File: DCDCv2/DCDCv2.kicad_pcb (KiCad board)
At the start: 4 copper layers, 137.2 x 79 mm, 58 parts, among them M1 CSD18513Q5A, M1_2 CSD18513Q5A, M2 CSD18531Q5A, M3 CSD18533Q5A, M3_2 CSD18533Q5A, M4 CSD19534Q5A, M4_2 CSD19534Q5A, U1 LM5175PWPR

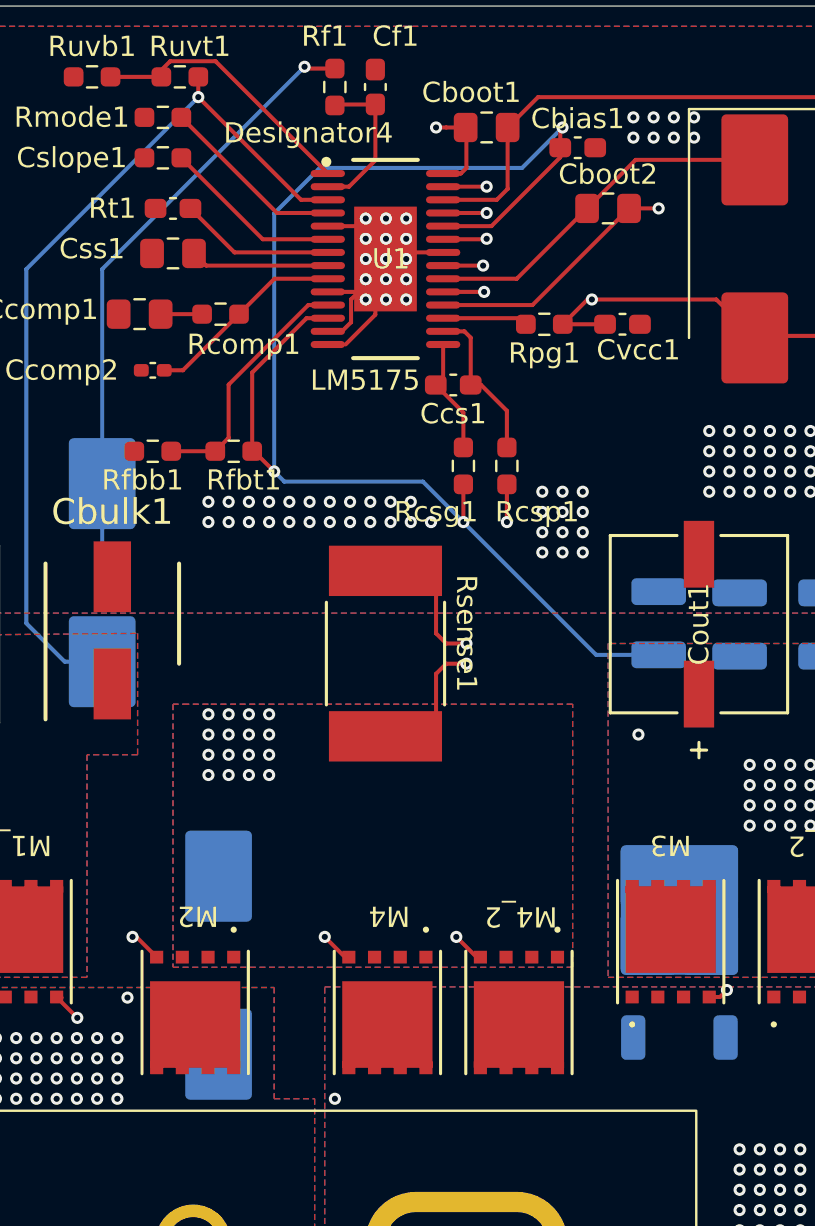
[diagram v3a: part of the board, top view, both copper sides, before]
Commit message: changed sw1 and sw2 to BCu layer
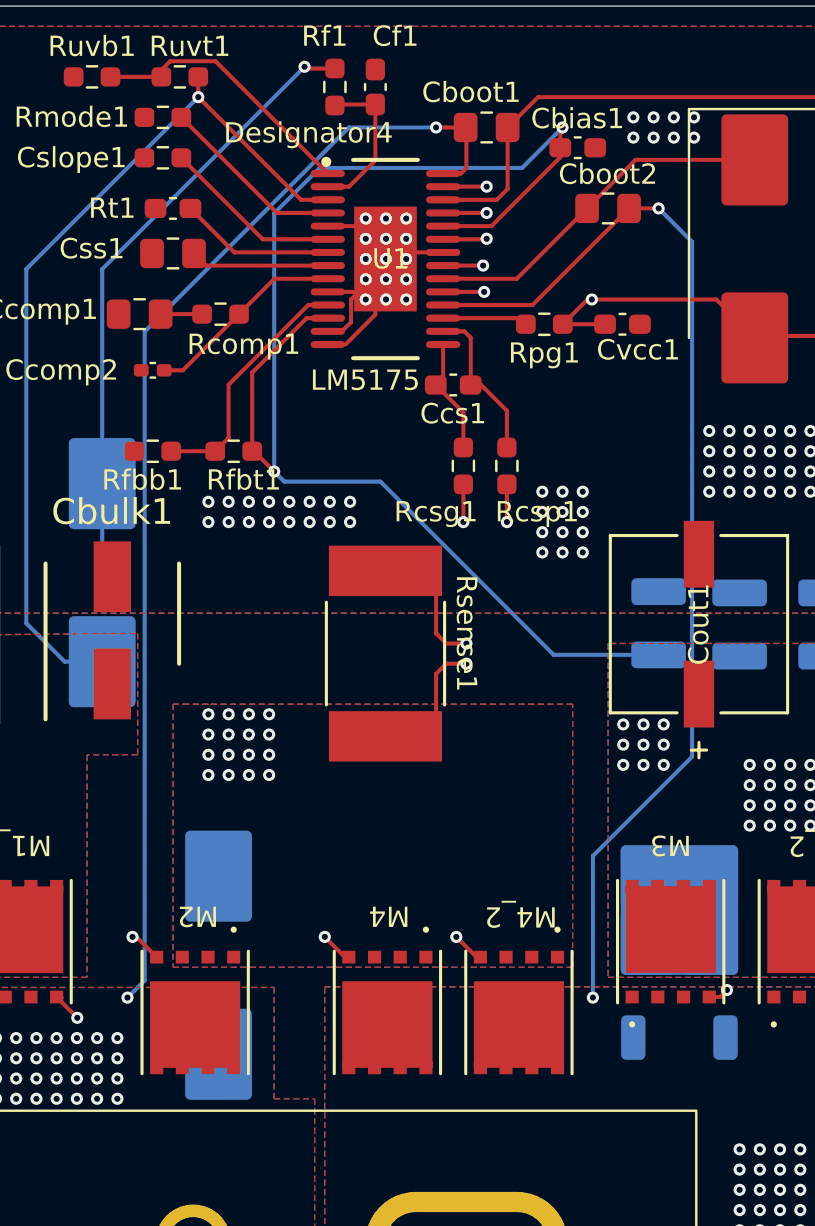
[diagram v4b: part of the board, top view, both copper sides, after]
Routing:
- net /sw2: track 88.0 -> 54.3 mm
- net /sw1: track 54.8 -> 56.6 mm
- net Vout: vias 99 -> 107
- net GND: vias 380 -> 373
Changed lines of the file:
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@@
 	)
 	(via micro
-		(at 95 54.5)
-		(size 0.6)
-		(drill 0.3)
-		(layers "F.Cu" "B.Cu")
-		(free yes)
-		(net 1)
-	)
-	(via micro
 		(at 39.25 50.5)
 		(size 0.6)
@@
 	)
 	(via micro
-		(at 93 54.5)
-		(size 0.6)
-		(drill 0.3)
-		(layers "F.Cu" "B.Cu")
-		(free yes)
-		(net 1)
-	)
-	(via micro
 		(at 147.75 52)
 		(size 0.6)
@@
 	)
 	(via micro
-		(at 96 54.5)
-		(size 0.6)
-		(drill 0.3)
-		(layers "F.Cu" "B.Cu")
-		(free yes)
-		(net 1)
-	)
-	(via micro
 		(at 52.25 52.5)
 		(size 0.6)
@@
 	)
 	(via micro
-		(at 94 54.5)
-		(size 0.6)
-		(drill 0.3)
-		(layers "F.Cu" "B.Cu")
-		(free yes)
-		(net 1)
-	)
-	(via micro
 		(at 47.25 52.5)
 		(size 0.6)
@@
 	)
 	(via micro
-		(at 94 53.5)
-		(size 0.6)
-		(drill 0.3)
-		(layers "F.Cu" "B.Cu")
-		(free yes)
-		(net 1)
-	)
-	(via micro
 		(at 49.25 52.5)
 		(size 0.6)
@@
 	)
 	(via micro
-		(at 95 53.5)
-		(size 0.6)
-		(drill 0.3)
-		(layers "F.Cu" "B.Cu")
-		(free yes)
-		(net 1)
-	)
-	(via micro
 		(at 113.75 53)
 		(size 0.6)
@@
 	)
 	(via micro
-		(at 93 53.5)
-		(size 0.6)
-		(drill 0.3)
-		(layers "F.Cu" "B.Cu")
-		(free yes)
-		(net 1)
-	)
-	(via micro
 		(at 114.75 52)
 		(size 0.6)
@@
 		(size 0.6)
 		(drill 0.3)
-		(layers "F.Cu" "In2.Cu")
+		(layers "F.Cu" "B.Cu")
 		(free yes)
 		(net 3)
@@
 		(size 0.6)
 		(drill 0.3)
-		(layers "F.Cu" "In2.Cu")
+		(layers "F.Cu" "B.Cu")
 		(net 3)
 	)
@@
 	)
 	(segment
-		(start 80.1 68.65)
-		(end 80.1 77.1)
-		(width 0.2)
-		(layer "In2.Cu")
-		(net 3)
-	)
-	(segment
-		(start 82.25 49)
-		(end 82.25 66.5)
+		(start 96.25 35)
+		(end 91.934314 35)
 		(width 0.2)
-		(layer "In2.Cu")
+		(layer "B.Cu")
 		(net 3)
 	)
 	(segment
-		(start 96.25 35)
-		(end 82.25 49)
+		(start 91.934314 35)
+		(end 81.85 45.084314)
 		(width 0.2)
-		(layer "In2.Cu")
+		(layer "B.Cu")
 		(net 3)
 	)
 	(segment
-		(start 82.25 66.5)
-		(end 80.1 68.65)
+		(start 81.85 45.084314)
+		(end 81.85 77.15)
 		(width 0.2)
-		(layer "In2.Cu")
+		(layer "B.Cu")
 		(net 3)
 	)
 	(segment
-		(start 80.1 77.1)
+		(start 81.85 77.15)
 		(end 81 78)
 		(width 0.2)
-		(layer "In2.Cu")
+		(layer "B.Cu")
 		(net 3)
 	)
@@
 		(size 0.6)
 		(drill 0.3)
-		(layers "F.Cu" "In2.Cu")
+		(layers "F.Cu" "B.Cu")
 		(net 5)
 	)
@@
 	)
 	(via micro
-		(at 91.25 83)
+		(at 104 78)
 		(size 0.6)
 		(drill 0.3)
-		(layers "F.Cu" "In2.Cu")
+		(layers "F.Cu" "B.Cu")
 		(free yes)
 		(net 5)
@@
 	)
 	(segment
-		(start 80.5 75.75)
-		(end 80.5 68.815686)
-		(width 0.2)
-		(layer "In2.Cu")
-		(net 5)
-	)
-	(segment
-		(start 80.5 68.815686)
-		(end 82.65 66.665686)
-		(width 0.2)
-		(layer "In2.Cu")
-		(net 5)
-	)
-	(segment
-		(start 82.65 66.665686)
-		(end 82.65 50.1)
-		(width 0.2)
-		(layer "In2.Cu")
-		(net 5)
-	)
-	(segment
-		(start 102.25 39.5)
-		(end 102.75 39)
-		(width 0.2)
-		(layer "In2.Cu")
-		(net 5)
-	)
-	(segment
-		(start 101.25 47)
-		(end 102.25 46)
-		(width 0.2)
-		(layer "In2.Cu")
-		(net 5)
-	)
-	(segment
-		(start 91.25 83)
-		(end 89.25 81)
-		(width 0.2)
-		(layer "In2.Cu")
-		(net 5)
-	)
-	(segment
-		(start 88.75 77)
-		(end 81.75 77)
-		(width 0.2)
-		(layer "In2.Cu")
-		(net 5)
-	)
-	(segment
-		(start 102.25 46)
-		(end 102.25 39.5)
-		(width 0.2)
-		(layer "In2.Cu")
-		(net 5)
-	)
-	(segment
-		(start 89.25 77.5)
-		(end 88.75 77)
-		(width 0.2)
-		(layer "In2.Cu")
-		(net 5)
-	)
-	(segment
-		(start 82.65 50.1)
-		(end 85.75 47)
-		(width 0.2)
-		(layer "In2.Cu")
-		(net 5)
-	)
-	(segment
-		(start 102.75 39)
+		(start 108.9 40.65)
 		(end 107.25 39)
 		(width 0.2)
-		(layer "In2.Cu")
+		(layer "B.Cu")
 		(net 5)
 	)
 	(segment
-		(start 81.75 77)
-		(end 80.5 75.75)
+		(start 104 71)
+		(end 108.9 66.1)
 		(width 0.2)
-		(layer "In2.Cu")
+		(layer "B.Cu")
 		(net 5)
 	)
 	(segment
-		(start 89.25 81)
-		(end 89.25 77.5)
+		(start 104 78)
+		(end 104 71)
 		(width 0.2)
-		(layer "In2.Cu")
+		(layer "B.Cu")
 		(net 5)
 	)
 	(segment
-		(start 85.75 47)
-		(end 101.25 47)
+		(start 108.9 66.1)
+		(end 108.9 40.65)
 		(width 0.2)
-		(layer "In2.Cu")
+		(layer "B.Cu")
 		(net 5)
 	)
@@
 		(net 26)
 	)
-	(via
+	(via micro
 		(at 102.5 35)
 		(size 0.6)
@@
 	)
 	(via micro
+		(at 107.5 66.5)
+		(size 0.6)
+		(drill 0.3)
+		(layers "F.Cu" "B.Cu")
+		(free yes)
+		(net 26)
+	)
+	(via micro
 		(at 128.75 68.5)
 		(size 0.6)
@@
 	)
 	(via micro
+		(at 105.5 65.5)
+		(size 0.6)
+		(drill 0.3)
+		(layers "F.Cu" "B.Cu")
+		(free yes)
+		(net 26)
+	)
+	(via micro
 		(at 118.75 67.5)
 		(size 0.6)
@@
 	)
 	(via micro
-		(at 130.75 68.5)
+		(at 105.5 66.5)
 		(size 0.6)
 		(drill 0.3)
@@
 	)
 	(via micro
-		(at 133.75 68.5)
+		(at 130.75 68.5)
 		(size 0.6)
 		(drill 0.3)
@@
 	)
 	(via micro
-		(at 112.75 69.5)
+		(at 133.75 68.5)
 		(size 0.6)
 		(drill 0.3)
@@
 	)
 	(via micro
-		(at 121.75 69.5)
+		(at 112.75 69.5)
 		(size 0.6)
 		(drill 0.3)
@@
 	)
 	(via micro
-		(at 106.25 65)
+		(at 121.75 69.5)
 		(size 0.6)
 		(drill 0.3)
-		(layers "F.Cu" "In1.Cu")
+		(layers "F.Cu" "B.Cu")
 		(free yes)
 		(net 26)
@@
 	)
 	(via micro
+		(at 106.5 65.5)
+		(size 0.6)
+		(drill 0.3)
+		(layers "F.Cu" "B.Cu")
+		(free yes)
+		(net 26)
+	)
+	(via micro
 		(at 133.75 67.5)
 		(size 0.6)
@@
 	)
 	(via micro
+		(at 107.5 64.5)
+		(size 0.6)
+		(drill 0.3)
+		(layers "F.Cu" "B.Cu")
+		(free yes)
+		(net 26)
+	)
+	(via micro
 		(at 132.75 67.5)
 		(size 0.6)
@@
 	)
 	(via micro
+		(at 105.5 64.5)
+		(size 0.6)
+		(drill 0.3)
+		(layers "F.Cu" "B.Cu")
+		(free yes)
+		(net 26)
+	)
+	(via micro
+		(at 106.5 66.5)
+		(size 0.6)
+		(drill 0.3)
+		(layers "F.Cu" "B.Cu")
+		(free yes)
+		(net 26)
+	)
+	(via micro
 		(at 120.75 66.5)
 		(size 0.6)
@@
 	)
 	(via micro
+		(at 107.5 65.5)
+		(size 0.6)
+		(drill 0.3)
+		(layers "F.Cu" "B.Cu")
+		(free yes)
+		(net 26)
+	)
+	(via micro
 		(at 111.75 67.5)
 		(size 0.6)
@@
 	)
 	(via micro
+		(at 106.5 64.5)
+		(size 0.6)
+		(drill 0.3)
+		(layers "F.Cu" "B.Cu")
+		(free yes)
+		(net 26)
+	)
+	(via micro
 		(at 130.75 69.5)
 		(size 0.6)
@@
 	)
 	(segment
-		(start 95.598529 52.5)
-		(end 104.161029 61.0625)
+		(start 88.75 52.5)
+		(end 93.5 52.5)
 		(width 0.2)
 		(layer "B.Cu")
@@
 	)
 	(segment
-		(start 104.161029 61.0625)
-		(end 107.25 61.0625)
+		(start 93.5 52.5)
+		(end 102.0625 61.0625)
 		(width 0.2)
 		(layer "B.Cu")
@@
 	)
 	(segment
-		(start 88.25 52)
-		(end 88.75 52.5)
+		(start 90.5 37)
+		(end 88.25 39.25)
 		(width 0.2)
 		(layer "B.Cu")
@@
 	)
 	(segment
-		(start 90.5 37)
-		(end 88.25 39.25)
+		(start 102.0625 61.0625)
+		(end 107.25 61.0625)
 		(width 0.2)
 		(layer "B.Cu")
@@
 	)
 	(segment
-		(start 88.75 52.5)
-		(end 95.598529 52.5)
+		(start 88.25 52)
+		(end 88.75 52.5)
 		(width 0.2)
 		(layer "B.Cu")

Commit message: finished PCB layout
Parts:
- added GND: TestPoint_THTPad_D2.0mm_Drill1.0mm, TestPoint:TestPoint_THTPad_D2.0mm_Drill1.0mm, F.Cu at (41.5, 46.0)
- added GND: TestPoint_THTPad_D2.0mm_Drill1.0mm, TestPoint:TestPoint_THTPad_D2.0mm_Drill1.0mm, F.Cu at (133.5, 46.0)
- added SW1: TestPoint_THTPad_D2.0mm_Drill1.0mm, TestPoint:TestPoint_THTPad_D2.0mm_Drill1.0mm, F.Cu at (69.5, 104.5)
- added SW2: TestPoint_THTPad_D2.0mm_Drill1.0mm, TestPoint:TestPoint_THTPad_D2.0mm_Drill1.0mm, F.Cu at (112.5, 104.5)
- added Vin: TestPoint_THTPad_D2.0mm_Drill1.0mm, TestPoint:TestPoint_THTPad_D2.0mm_Drill1.0mm, F.Cu at (42.0, 80.0)
- added Vout: TestPoint_THTPad_D2.0mm_Drill1.0mm, TestPoint:TestPoint_THTPad_D2.0mm_Drill1.0mm, F.Cu at (124.5, 82.0)
- moved Cbulk1 49.3 mm to (31.0, 59.4)
- moved Cf1 12.8 mm to (80.6, 30.8), turned to 180 degrees
- moved G*** 11.5 mm to (51.0, 93.0)
- moved Cin1 10.3 mm to (60.5, 59.5)
- moved Cin_2 10.3 mm to (50.5, 59.5)
- moved Cin_3 10.3 mm to (80.5, 59.5)
- moved Cin_4 10.3 mm to (40.5, 59.5)
- moved Cin_5 10.3 mm to (70.5, 59.5)
- moved Rfbb1 3.15 mm to (80.1, 48.7)
- moved Cslope1 2.86 mm to (80.5, 38.2)
- moved Ccomp2 2.65 mm to (80.3, 45.2)
- moved Css1 2.65 mm to (80.7, 40.5)
- moved Rt1 2.15 mm to (80.6, 36.4)
- moved Rmode1 2.05 mm to (80.7, 34.4)
- moved Rcomp1 1.93 mm to (87.0, 42.9)
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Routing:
- net GND: track 33.1 -> 45.9 mm
- net Net-(U1-VIN): track 7.67 -> 17.0 mm
- net /sw2: track 54.3 -> 57.4 mm
- net Net-(U1-FB): track 12.3 -> 15.4 mm
- net Net-(U1-SLOPE): track 7.69 -> 10.8 mm
- net Net-(U1-SS): track 6.86 -> 9.71 mm
- net Net-(Ccomp1-Pad1): track 2.05 -> 4.43 mm
- net /sw1: track 56.6 -> 58.8 mm
- net Net-(U1-RT_SYNC): track 8.90 -> 11.1 mm
- net Net-(U1-MODE): track 9.19 -> 11.3 mm
- net Net-(U1-EN): track 13.4 -> 11.6 mm
- net Net-(U1-COMP): track 10.7 -> 12.0 mm
- net Vin: track 44.4 -> 45.3 mm, vias 97 -> 98
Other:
- board size 137.2 x 79 mm -> 137.8 x 82.6 mm
- board text added: "{dblquote}pissman 8{dblquote}"
- board text removed: "ok"

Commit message: final touches, ready for order
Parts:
- Vin (15 to 28V): renamed from Vin1
- Vout (24V): renamed from Vout1
- moved Rfbt1 2.00 mm to (86.2, 49.0)
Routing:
- net Net-(U1-FB): track 15.4 -> 12.5 mm
- net /sw2: track 57.4 -> 58.7 mm
